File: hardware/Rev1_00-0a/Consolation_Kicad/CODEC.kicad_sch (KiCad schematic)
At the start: 27 parts, among them J2 SJ-3524-SMT-TR, U4 ECS-2016MVQ-120-BP-TR, U5 NAU88C22YG

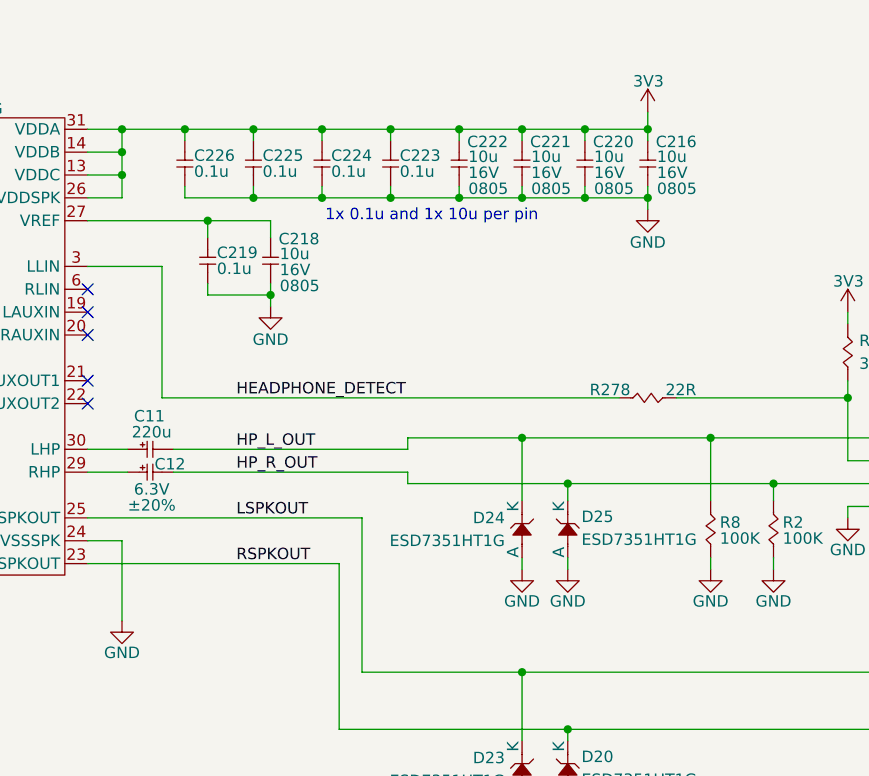
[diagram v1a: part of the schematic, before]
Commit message: Continue preliminary placement To do : Power supplies + Type C charger
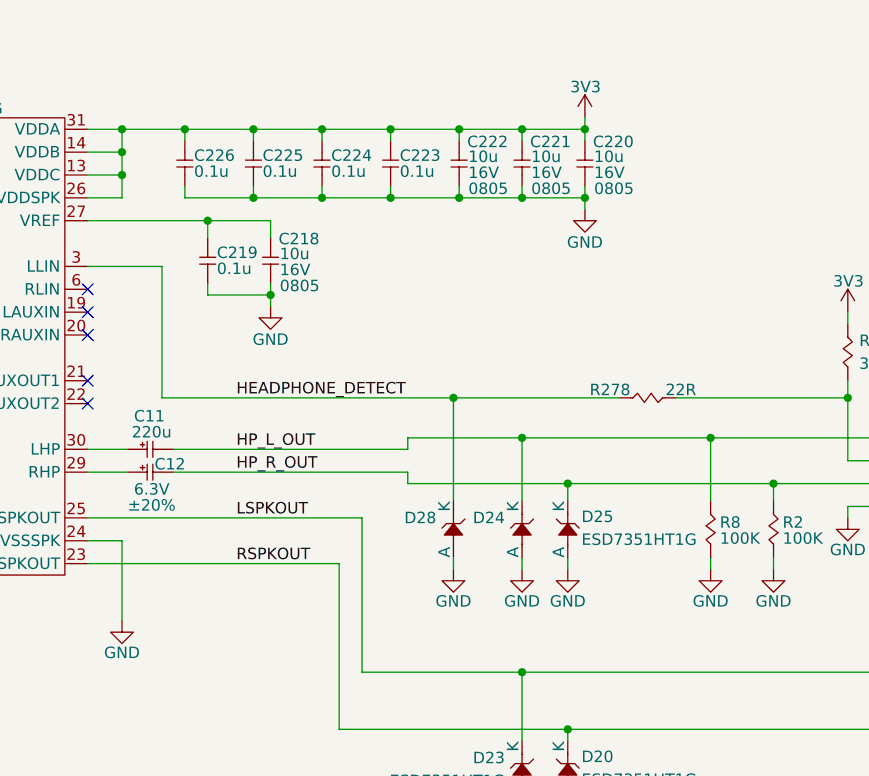
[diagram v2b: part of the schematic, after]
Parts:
- removed C216: 10u, footprint:CAP_NONPOL_0805, symbol KicadCompDb:Capacitors/CAP_CER_SMT_00004
- added D28: ESD7351HT1G, footprint:SOD-323, symbol KicadCompDb:ESD Diodes/ESD_DIODE_00006
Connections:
- net GND: now also D28.2 (A)
- net HEADPHONE_DETECT: now also D28.1 (K)
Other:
- note removed: "1x 0.1u and 1x 10u per pin"

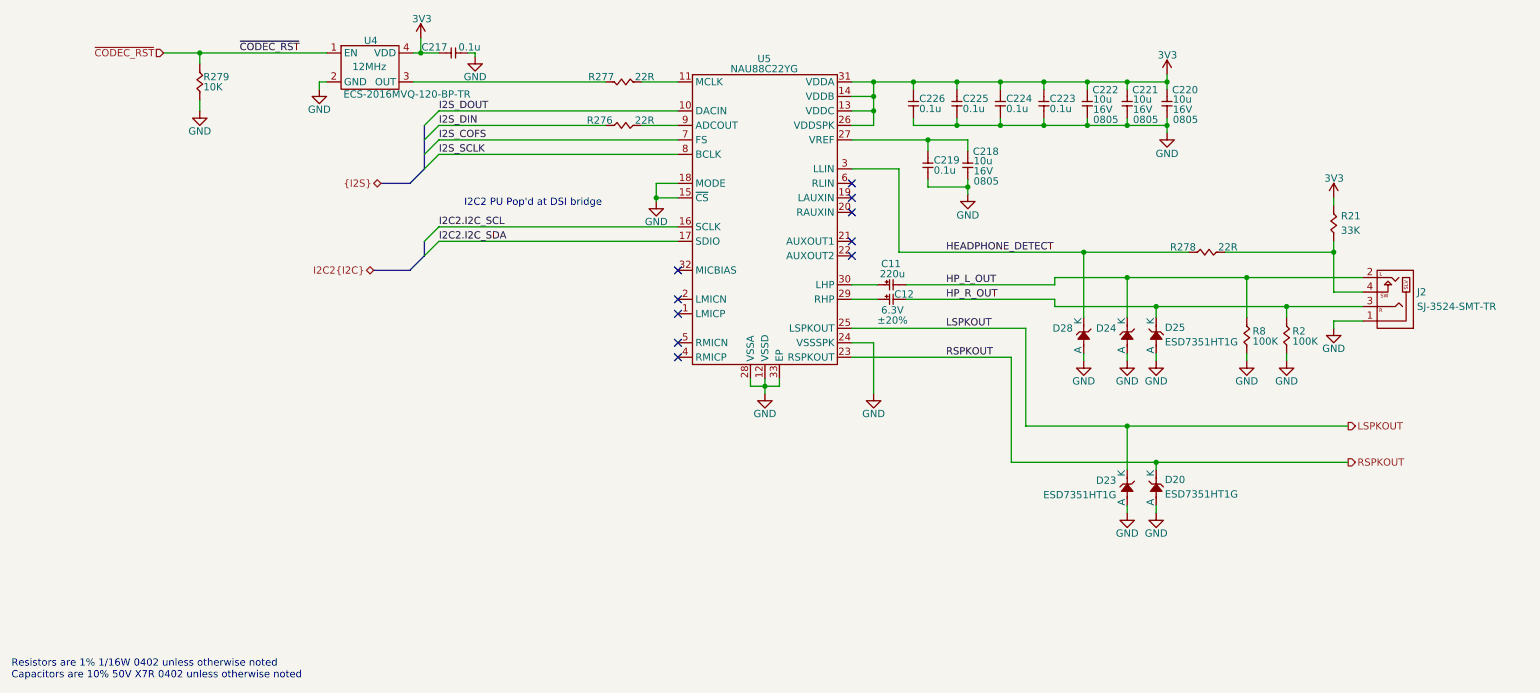
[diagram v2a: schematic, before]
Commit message: Preliminary placement done Add test points to PCB
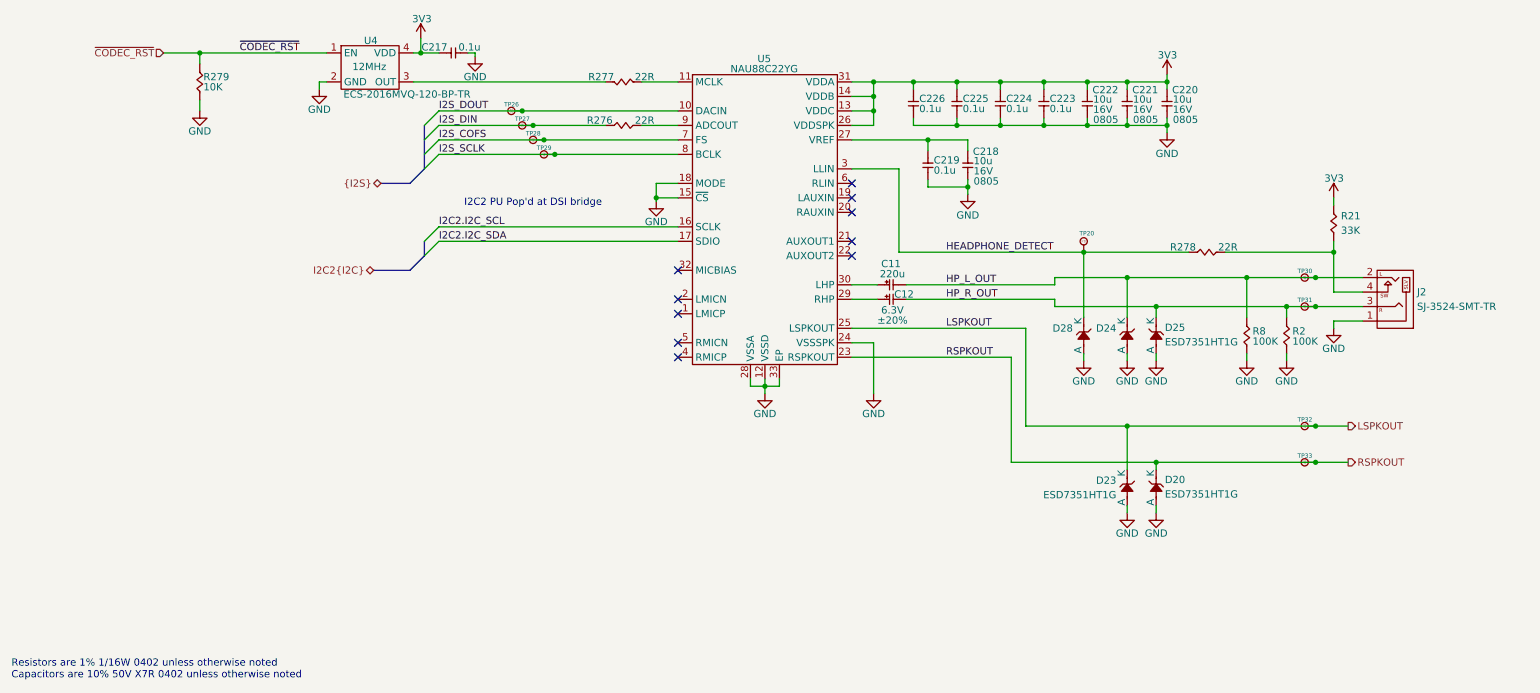
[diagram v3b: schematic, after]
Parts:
- added TP20, TP26, TP27, TP28, TP29, TP30, TP31, TP32, TP33: 75 mils, footprint:SMT_TP_75_MILS, symbol KicadCompDb:Test Point/TP_00004
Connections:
- net HEADPHONE_DETECT: now also TP20.1
- net HP_L_OUT: now also TP30.1
- net HP_R_OUT: now also TP31.1
- net I2S_COFS: now also TP28.1
- net I2S_DIN: now also TP27.1
- net I2S_DOUT: now also TP26.1
- net I2S_SCLK: now also TP29.1
- net LSPKOUT: now also TP32.1
- net RSPKOUT: now also TP33.1

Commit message: Routing Adjust PinMux to ease routing
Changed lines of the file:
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@@
 	(title_block
 		(title "Consolation [Console Emulation]")
-		(date "2026-10-12")
+		(date "2026-10-25")
 		(rev "1.00-0A")
 		(comment 1 "Jean-Francois Bilodeau")
@@
 	(bus
 		(pts
-			(xy 77.47 85.725) (xy 82.55 85.725)
+			(xy 76.2 85.725) (xy 82.55 85.725)
 		)
 		(stroke
@@
 	(hierarchical_label "{I2S}"
 		(shape bidirectional)
-		(at 77.47 85.725 180)
+		(at 76.2 85.725 180)
 		(effects
 			(font
